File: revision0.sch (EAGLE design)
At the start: 92 parts, among them IC1 MSP430FR698X(1)80-PIN_PN, IC3 FT232RL

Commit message: Move GPS-TIMEPULSE sig to interrupt capable input (P2.1)
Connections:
- net GPS-TIMEPULSE: now also IC1.P2.1/UCA0SOMI/UCA0RXD/TB0.5/DMAE0/S15; no longer IC1.P9.1/ESICH1/ESITEST1/A9/C9
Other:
- moved on the sheet: C15, S4
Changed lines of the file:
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@@
 <instance part="GND13" gate="1" x="-165.1" y="12.7" rot="R270"/>
 <instance part="R3" gate="G$1" x="-182.88" y="-45.72" rot="R90"/>
-<instance part="C15" gate="G$1" x="-182.88" y="-81.28" rot="MR0"/>
-<instance part="GND14" gate="1" x="-182.88" y="-96.52"/>
+<instance part="C15" gate="G$1" x="-182.88" y="-106.68" rot="MR0"/>
+<instance part="GND14" gate="1" x="-182.88" y="-121.92"/>
 <instance part="U$3" gate="G$1" x="259.08" y="-60.96"/>
 <instance part="U$2" gate="G$1" x="251.46" y="187.96"/>
@@
 <instance part="R32" gate="G$1" x="-203.2" y="22.86" rot="R180"/>
 <instance part="C20" gate="G$1" x="-314.96" y="132.08" rot="R180"/>
-<instance part="S4" gate="1" x="-195.58" y="-81.28" rot="MR180"/>
+<instance part="S4" gate="1" x="-195.58" y="-106.68" rot="MR180"/>
 <instance part="R6" gate="G$1" x="-414.02" y="99.06" rot="R270"/>
 <instance part="R22" gate="G$1" x="-419.1" y="106.68" rot="R270"/>
@@
 <pinref part="C15" gate="G$1" pin="2"/>
 <pinref part="GND14" gate="1" pin="GND"/>
-<wire x1="-182.88" y1="-93.98" x2="-182.88" y2="-88.9" width="0.1524" layer="91"/>
+<wire x1="-182.88" y1="-119.38" x2="-182.88" y2="-114.3" width="0.1524" layer="91"/>
 <pinref part="S4" gate="1" pin="S"/>
-<wire x1="-182.88" y1="-88.9" x2="-182.88" y2="-86.36" width="0.1524" layer="91"/>
-<wire x1="-195.58" y1="-86.36" x2="-195.58" y2="-88.9" width="0.1524" layer="91"/>
-<wire x1="-195.58" y1="-88.9" x2="-193.04" y2="-88.9" width="0.1524" layer="91"/>
+<wire x1="-182.88" y1="-114.3" x2="-182.88" y2="-111.76" width="0.1524" layer="91"/>
+<wire x1="-195.58" y1="-111.76" x2="-195.58" y2="-114.3" width="0.1524" layer="91"/>
+<wire x1="-195.58" y1="-114.3" x2="-193.04" y2="-114.3" width="0.1524" layer="91"/>
 <pinref part="S4" gate="1" pin="S1"/>
-<wire x1="-193.04" y1="-88.9" x2="-193.04" y2="-86.36" width="0.1524" layer="91"/>
-<wire x1="-193.04" y1="-88.9" x2="-182.88" y2="-88.9" width="0.1524" layer="91"/>
-<junction x="-193.04" y="-88.9"/>
-<junction x="-182.88" y="-88.9"/>
+<wire x1="-193.04" y1="-114.3" x2="-193.04" y2="-111.76" width="0.1524" layer="91"/>
+<wire x1="-193.04" y1="-114.3" x2="-182.88" y2="-114.3" width="0.1524" layer="91"/>
+<junction x="-193.04" y="-114.3"/>
+<junction x="-182.88" y="-114.3"/>
 </segment>
 <segment>
@@
 <wire x1="-182.88" y1="-53.34" x2="-182.88" y2="-50.8" width="0.1524" layer="91"/>
 <pinref part="C15" gate="G$1" pin="1"/>
-<wire x1="-182.88" y1="-53.34" x2="-182.88" y2="-73.66" width="0.1524" layer="91"/>
+<wire x1="-182.88" y1="-53.34" x2="-182.88" y2="-99.06" width="0.1524" layer="91"/>
 <junction x="-182.88" y="-53.34"/>
-<wire x1="-182.88" y1="-73.66" x2="-182.88" y2="-78.74" width="0.1524" layer="91"/>
+<wire x1="-182.88" y1="-99.06" x2="-182.88" y2="-104.14" width="0.1524" layer="91"/>
 <wire x1="-233.68" y1="-53.34" x2="-182.88" y2="-53.34" width="0.1524" layer="91"/>
 <label x="-238.76" y="-53.34" size="1.778" layer="95"/>
 <pinref part="S4" gate="1" pin="P"/>
-<wire x1="-195.58" y1="-76.2" x2="-195.58" y2="-73.66" width="0.1524" layer="91"/>
+<wire x1="-195.58" y1="-101.6" x2="-195.58" y2="-99.06" width="0.1524" layer="91"/>
 <pinref part="S4" gate="1" pin="P1"/>
-<wire x1="-195.58" y1="-73.66" x2="-193.04" y2="-73.66" width="0.1524" layer="91"/>
-<wire x1="-193.04" y1="-73.66" x2="-193.04" y2="-76.2" width="0.1524" layer="91"/>
-<wire x1="-193.04" y1="-73.66" x2="-182.88" y2="-73.66" width="0.1524" layer="91"/>
-<junction x="-193.04" y="-73.66"/>
-<junction x="-182.88" y="-73.66"/>
+<wire x1="-195.58" y1="-99.06" x2="-193.04" y2="-99.06" width="0.1524" layer="91"/>
+<wire x1="-193.04" y1="-99.06" x2="-193.04" y2="-101.6" width="0.1524" layer="91"/>
+<wire x1="-193.04" y1="-99.06" x2="-182.88" y2="-99.06" width="0.1524" layer="91"/>
+<junction x="-193.04" y="-99.06"/>
+<junction x="-182.88" y="-99.06"/>
 </segment>
 <segment>
@@
 <segment>
 <wire x1="-233.68" y1="-71.12" x2="-160.02" y2="-71.12" width="0.1524" layer="91"/>
-<label x="96.52" y="-43.18" size="1.778" layer="95"/>
 <wire x1="-160.02" y1="-71.12" x2="-160.02" y2="-68.58" width="0.1524" layer="91"/>
 <pinref part="IC1" gate="G$1" pin="P2.3/UCA0STE/TB0OUTH/S17"/>
@@
 </segment>
 <segment>
-<wire x1="-5.08" y1="-45.72" x2="93.98" y2="-45.72" width="0.1524" layer="91"/>
-<label x="96.52" y="-48.26" size="1.778" layer="95"/>
-<pinref part="IC1" gate="G$1" pin="P9.1/ESICH1/ESITEST1/A9/C9"/>
-<wire x1="-5.08" y1="-45.72" x2="-7.62" y2="-43.18" width="0.1524" layer="91"/>
-</segment>
-</net>
+<wire x1="-233.68" y1="-73.66" x2="-154.94" y2="-73.66" width="0.1524" layer="91"/>
+<label x="-238.76" y="-73.66" size="1.778" layer="95"/>
+<pinref part="IC1" gate="G$1" pin="P2.1/UCA0SOMI/UCA0RXD/TB0.5/DMAE0/S15"/>
+</segment>
+</net>

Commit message: Redesign a lot GPS RF part, CPU pins
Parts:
- removed R17: 0, tagps:R-EU_R0805
- removed TP-GPSTIMEPULSE: TPSQPAD1-20, tagps:TPSQPAD1-20
- added SBW: (no value), tagps:PINHD-1X3
- added SV1: (no value), tagps:FE07W
- added TP1: TPSQTP16R, tagps:TPSQTP16R
- JP1: value JTAG -> (none); device tagps:PINHD-2X7 -> tagps:PINHD-1X7/90
- JP2: device tagps:JP2E -> tagps:JP1Q
- TP-ADC-VREF, TP-GPSPWR, TP-GPSRX, TP-GPSTX: value TPSQPAD1-20 -> TPSQTP10R; device tagps:TPSQPAD1-20 -> tagps:TPSQTP10R
- TP-PWRBATT, TP-PWRUSB, TP-USBRX, TP-USBTX, TP-VCC, TP-VCCSTAT: value TPSQPAD1-20 -> TPSQPAD1-13; device tagps:TPSQPAD1-20 -> tagps:TPSQPAD1-13
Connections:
- removed net VCC_TARGET: JP1.4, JP2.1
- removed net VCC_TOOL: JP1.2, JP2.3
- new net MB-GPS-RX: R23.2, SV1.6
- new net MB-GPS-TIMEPULSE: IC1.P2.1/UCA0SOMI/UCA0RXD/TB0.5/DMAE0/S15, SV1.3
- new net MB-GPS-TX: IC1.P3.5/UCA1SOMI/UCA1RXD/TB0.1/S20, SV1.5
- new net MB-GPS-WAKEUP: IC1.P9.0/ESICH0/ESITEST0/A8/C8, SV1.4
- new net MB_PWR_GPS_SENSE: IC1.P2.2/UCA0CLK/TB0.4/RTCCLK/S16, S2.3.1, SV1.2
- net ANTENNA: now also TP1.TP
- net GND: now also JP1.1, JP1.7, SBW.1, SV1.1, SV1.7; no longer JP1.9
- net GPS-RX: now also JP1.2; no longer R23.2
- net GPS-TIMEPULSE: now also JP1.5; no longer IC1.P2.1/UCA0SOMI/UCA0RXD/TB0.5/DMAE0/S15
- net GPS-TX: now also JP1.3; no longer IC1.P3.5/UCA1SOMI/UCA1RXD/TB0.1/S20
- net GPS-WAKEUP: now also JP1.4; no longer IC1.P9.0/ESICH0/ESITEST0/A8/C8
- net LED1: now also IC1.P7.7/TA1.2/TB0OUTH/S23; no longer IC1.P6.5/TB0.1/COM2/S35
- net LED2: now also IC1.P7.6/TA0.1/S24; no longer IC1.P6.6/TB0.2/COM3/S34
- net N$26: now also JP2.1; no longer R17.2
- net N$9: no longer TP-GPSTIMEPULSE.TP
- net PWR_GPS_SENSE: now also JP1.6; no longer IC1.P2.3/UCA0STE/TB0OUTH/S17, S2.3.1
- net SBW-TCK: now also SBW.3; no longer JP1.7
- net SBW-TDO/TDI: now also SBW.2; no longer JP1.1
- net SW-CFG-GPS: now also IC1.P3.7/UCA1STE/TB0.3/S18; no longer IC1.P7.0/TA0CLK/S13
- net SW-CHECK-BATT-MEM: now also IC1.P3.6/UCA1CLK/TB0.2/S19; no longer IC1.P2.0/UCA0SIMO/UCA0TXD/TB0.6/TB0CLK/S14
- net VCC: no longer R17.1
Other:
- moved on the sheet: C15, R23, R3, S2, S4

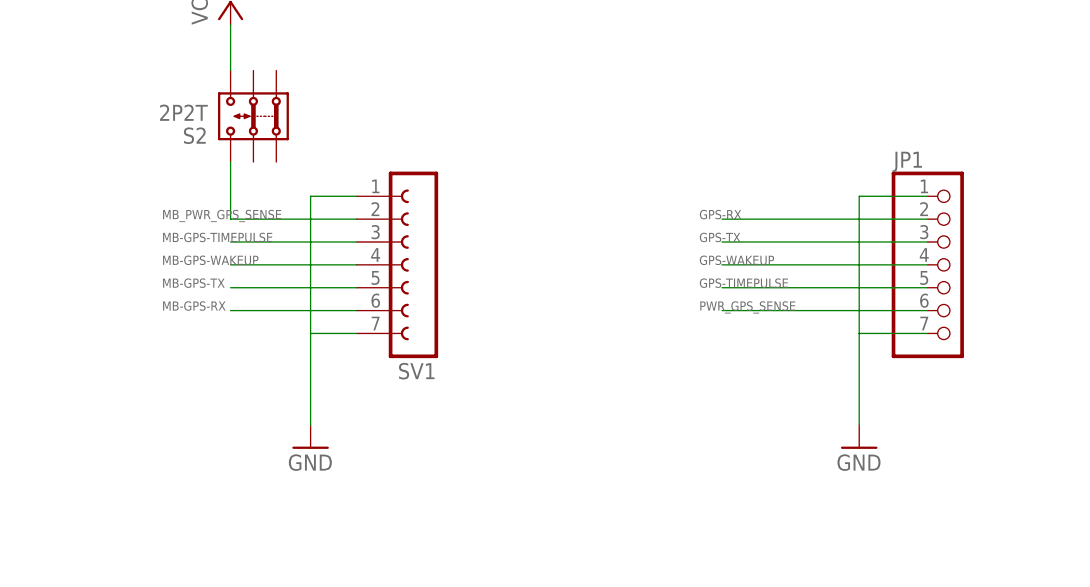
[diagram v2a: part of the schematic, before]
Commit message: Patch antenna module done
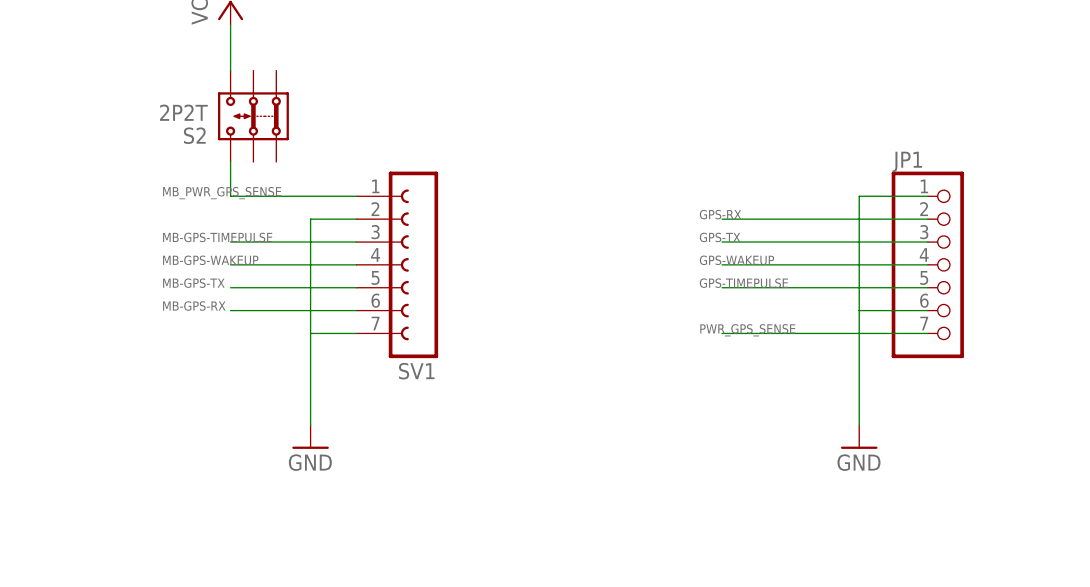
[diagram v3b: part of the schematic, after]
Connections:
- net GND: now also JP1.6, SV1.2; no longer JP1.7, SV1.1
- net MB_PWR_GPS_SENSE: now also SV1.1; no longer SV1.2
- net PWR_GPS_SENSE: now also JP1.7; no longer JP1.6
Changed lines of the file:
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@@
 <setting verticaltext="up"/>
 </settings>
-<grid distance="0.1" unitdist="inch" unit="inch" style="lines" multiple="1" display="no" altdistance="0.01" altunitdist="inch" altunit="inch"/>
+<grid distance="50" unitdist="mil" unit="mil" style="lines" multiple="1" display="yes" altdistance="0.01" altunitdist="inch" altunit="inch"/>
 <layers>
 <layer number="1" name="Top" color="4" fill="1" visible="no" active="no"/>
@@
 <part name="P+1" library="tagps" deviceset="VCC" device="" value="VCC"/>
 <part name="P+3" library="tagps" deviceset="VCC" device="" value="VCC"/>
-<part name="GND7" library="supply1" deviceset="GND" device=""/>
 <part name="C3" library="tagps" deviceset="C-EU" device="C0805" value="100n"/>
 <part name="C4" library="tagps" deviceset="C-EU" device="C0805" value="1u"/>
@@
 <part name="SBW" library="tagps" deviceset="PINHD-1X3" device=""/>
 <part name="JP1" library="tagps" deviceset="PINHD-1X7" device="/90"/>
-<part name="GND12" library="supply1" deviceset="GND" device=""/>
 <part name="JP2" library="tagps" deviceset="JP1Q" device=""/>
 <part name="SV1" library="tagps" deviceset="FE07W" device=""/>
 <part name="GND32" library="supply1" deviceset="GND" device=""/>
 <part name="TP1" library="tagps" deviceset="TPSQ" device="TP16R"/>
+<part name="GND7" library="supply1" deviceset="GND" device=""/>
+<part name="GND12" library="supply1" deviceset="GND" device=""/>
 </parts>
 <sheets>
@@
 <instance part="P+1" gate="VCC" x="-193.04" y="-35.56" rot="R90"/>
 <instance part="P+3" gate="VCC" x="180.34" y="73.66"/>
-<instance part="GND7" gate="1" x="281.94" y="-88.9"/>
 <instance part="C3" gate="G$1" x="-175.26" y="-25.4" rot="MR0"/>
 <instance part="C4" gate="G$1" x="-182.88" y="-25.4" rot="MR0"/>
@@
 <instance part="SBW" gate="A" x="-137.16" y="-96.52" rot="R180"/>
 <instance part="JP1" gate="A" x="260.35" y="44.45"/>
-<instance part="GND12" gate="1" x="250.19" y="24.13"/>
 <instance part="JP2" gate="A" x="276.86" y="212.09"/>
 <instance part="SV1" gate="G$1" x="201.93" y="44.45" rot="R180"/>
 <instance part="GND32" gate="1" x="189.23" y="24.13"/>
 <instance part="TP1" gate="G$1" x="226.06" y="-25.4" rot="R180"/>
+<instance part="GND7" gate="1" x="250.19" y="24.13"/>
+<instance part="GND12" gate="1" x="281.94" y="-88.9"/>
 </instances>
 <busses>
@@
 </segment>
 <segment>
-<wire x1="274.32" y1="-73.66" x2="281.94" y2="-73.66" width="0.1524" layer="91"/>
-<wire x1="281.94" y1="-73.66" x2="281.94" y2="-86.36" width="0.1524" layer="91"/>
-<pinref part="GND7" gate="1" pin="GND"/>
-<pinref part="U$3" gate="G$1" pin="GND"/>
-</segment>
-<segment>
 <pinref part="IC1" gate="G$1" pin="DVSS1"/>
 <wire x1="-154.94" y1="-25.4" x2="-170.18" y2="-25.4" width="0.1524" layer="91"/>
@@
 </segment>
 <segment>
-<pinref part="GND12" gate="1" pin="GND"/>
-<wire x1="257.81" y1="52.07" x2="250.19" y2="52.07" width="0.1524" layer="91"/>
-<wire x1="250.19" y1="52.07" x2="250.19" y2="36.83" width="0.1524" layer="91"/>
-<wire x1="250.19" y1="36.83" x2="250.19" y2="26.67" width="0.1524" layer="91"/>
-<wire x1="257.81" y1="36.83" x2="250.19" y2="36.83" width="0.1524" layer="91"/>
-<pinref part="JP1" gate="A" pin="1"/>
-<pinref part="JP1" gate="A" pin="7"/>
-</segment>
-<segment>
 <pinref part="SV1" gate="G$1" pin="7"/>
 <pinref part="GND32" gate="1" pin="GND"/>
 <wire x1="194.31" y1="36.83" x2="189.23" y2="36.83" width="0.1524" layer="91"/>
 <wire x1="189.23" y1="36.83" x2="189.23" y2="26.67" width="0.1524" layer="91"/>
-<pinref part="SV1" gate="G$1" pin="1"/>
-<wire x1="194.31" y1="52.07" x2="189.23" y2="52.07" width="0.1524" layer="91"/>
-<wire x1="189.23" y1="52.07" x2="189.23" y2="36.83" width="0.1524" layer="91"/>
+<wire x1="194.31" y1="49.53" x2="189.23" y2="49.53" width="0.1524" layer="91"/>
+<wire x1="189.23" y1="49.53" x2="189.23" y2="36.83" width="0.1524" layer="91"/>
+<pinref part="SV1" gate="G$1" pin="2"/>
+</segment>
+<segment>
+<wire x1="274.32" y1="-73.66" x2="281.94" y2="-73.66" width="0.1524" layer="91"/>
+<wire x1="281.94" y1="-73.66" x2="281.94" y2="-86.36" width="0.1524" layer="91"/>
+<pinref part="U$3" gate="G$1" pin="GND"/>
+<pinref part="GND12" gate="1" pin="GND"/>
+</segment>
+<segment>
+<wire x1="257.81" y1="52.07" x2="250.19" y2="52.07" width="0.1524" layer="91"/>
+<wire x1="250.19" y1="52.07" x2="250.19" y2="39.37" width="0.1524" layer="91"/>
+<pinref part="JP1" gate="A" pin="1"/>
+<pinref part="GND7" gate="1" pin="GND"/>
+<pinref part="JP1" gate="A" pin="6"/>
+<wire x1="250.19" y1="39.37" x2="250.19" y2="26.67" width="0.1524" layer="91"/>
+<wire x1="257.81" y1="39.37" x2="250.19" y2="39.37" width="0.1524" layer="91"/>
 </segment>
 </net>
@@
 </segment>
 <segment>
-<wire x1="234.95" y1="39.37" x2="257.81" y2="39.37" width="0.1524" layer="91"/>
-<label x="232.41" y="39.37" size="1.016" layer="95"/>
-<pinref part="JP1" gate="A" pin="6"/>
+<wire x1="234.95" y1="36.83" x2="257.81" y2="36.83" width="0.1524" layer="91"/>
+<label x="232.41" y="36.83" size="1.016" layer="95"/>
+<pinref part="JP1" gate="A" pin="7"/>
 </segment>
 </net>
@@
 </segment>
 <segment>
-<wire x1="180.34" y1="49.53" x2="194.31" y2="49.53" width="0.1524" layer="91"/>
-<label x="172.72" y="49.53" size="1.016" layer="95"/>
+<wire x1="180.34" y1="52.07" x2="194.31" y2="52.07" width="0.1524" layer="91"/>
+<label x="172.72" y="52.07" size="1.016" layer="95"/>
 <pinref part="S2" gate="G$1" pin="3.1"/>
-<wire x1="180.34" y1="49.53" x2="180.34" y2="55.88" width="0.1524" layer="91"/>
-<pinref part="SV1" gate="G$1" pin="2"/>
-</segment>
-</net>
+<wire x1="180.34" y1="52.07" x2="180.34" y2="55.88" width="0.1524" layer="91"/>
+<pinref part="SV1" gate="G$1" pin="1"/>
+</segment>
+</net>
